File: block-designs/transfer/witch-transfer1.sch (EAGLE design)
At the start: 13 parts, among them IC1 74LS73N, IC2 74S08N

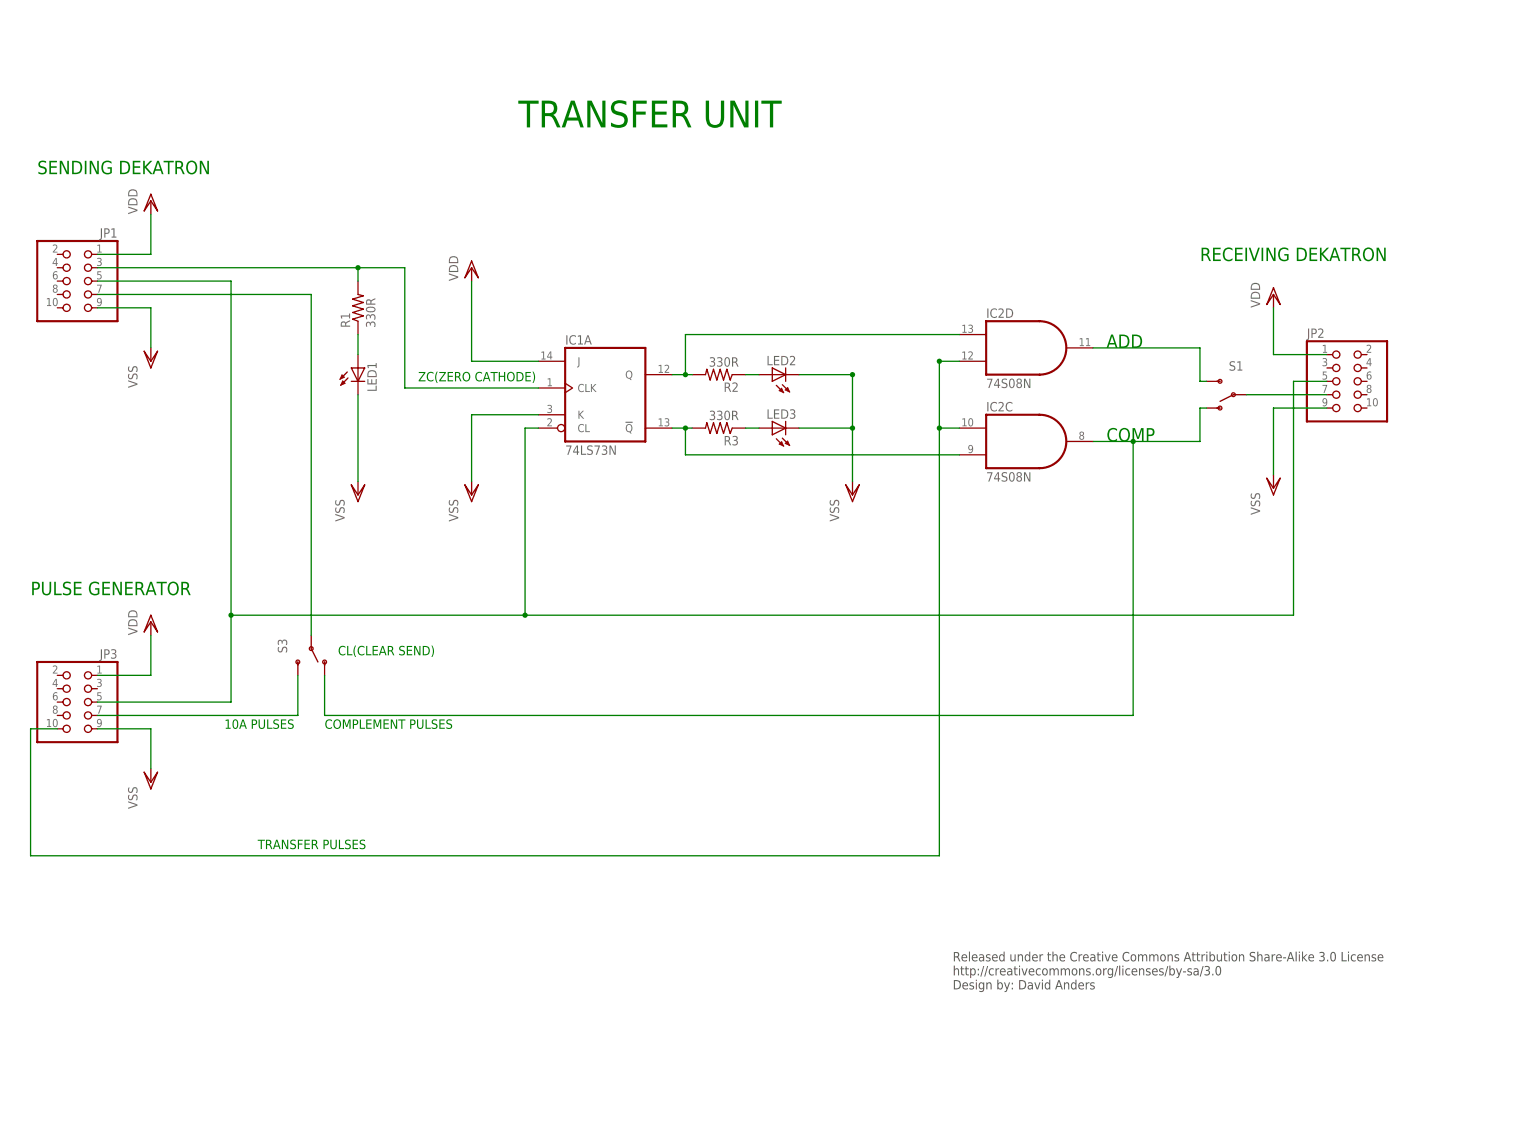
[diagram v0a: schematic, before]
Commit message: updated transfer block with board layout
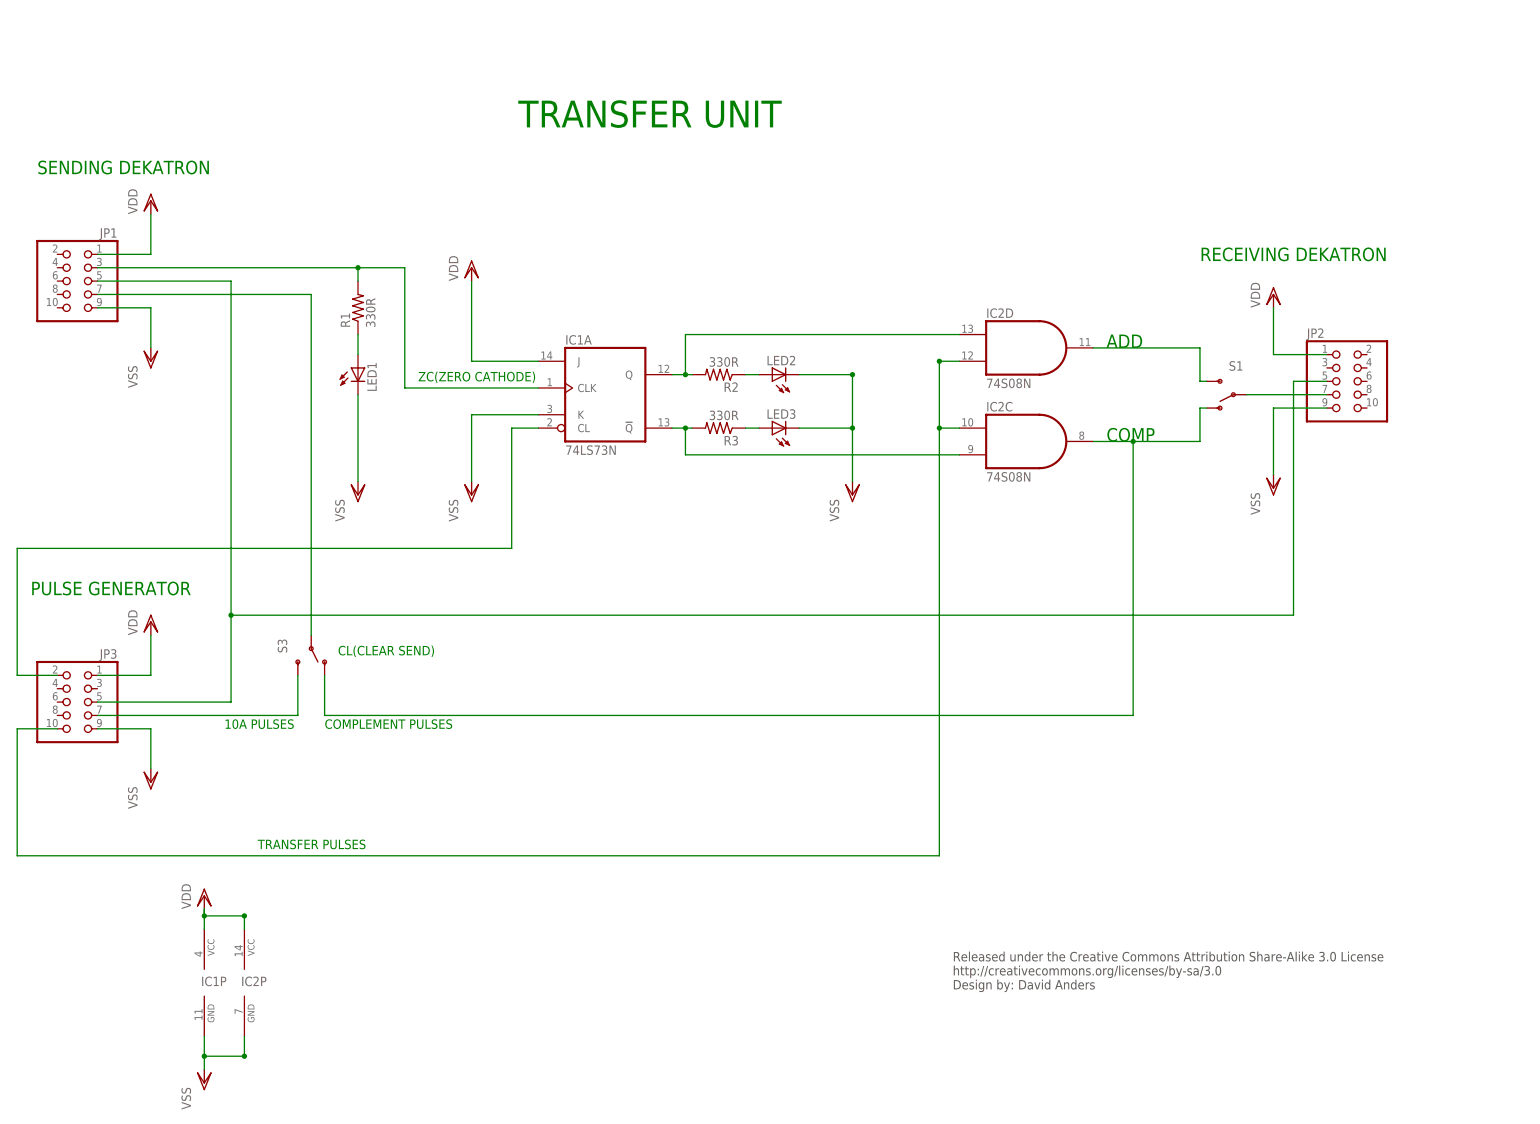
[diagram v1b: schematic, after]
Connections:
- new net N$10: IC1A.CL, JP3.2
- net N$32: no longer IC1A.CL
- net VDD: now also IC1P.VCC, IC2P.VCC
- net VSS: now also IC1P.GND, IC2P.GND
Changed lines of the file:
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@@
 <part name="R2" library="resistor" deviceset="R-US_" device="0204/5" value="330R"/>
 <part name="R3" library="resistor" deviceset="R-US_" device="0204/5" value="330R"/>
+<part name="VSS7" library="supply1" deviceset="VSS" device=""/>
+<part name="VDD5" library="supply1" deviceset="VDD" device=""/>
 </parts>
 <sheets>
@@
 <instance part="R2" gate="G$1" x="140.97" y="142.24" rot="R180"/>
 <instance part="R3" gate="G$1" x="140.97" y="132.08" rot="R180"/>
+<instance part="IC1" gate="P" x="43.18" y="26.67"/>
+<instance part="IC2" gate="P" x="50.8" y="26.67"/>
+<instance part="VSS7" gate="G$1" x="43.18" y="7.62"/>
+<instance part="VDD5" gate="G$1" x="43.18" y="43.18"/>
 </instances>
 <busses>
@@
 <net name="N$32" class="0">
 <segment>
-<pinref part="IC1" gate="A" pin="CL"/>
-<wire x1="106.68" y1="132.08" x2="104.14" y2="132.08" width="0.1524" layer="91"/>
 <pinref part="JP1" gate="A" pin="5"/>
 <wire x1="22.86" y1="160.02" x2="48.26" y2="160.02" width="0.1524" layer="91"/>
@@
 <wire x1="48.26" y1="160.02" x2="48.26" y2="96.52" width="0.1524" layer="91"/>
 <wire x1="48.26" y1="96.52" x2="48.26" y2="80.01" width="0.1524" layer="91"/>
-<wire x1="104.14" y1="132.08" x2="104.14" y2="96.52" width="0.1524" layer="91"/>
-<wire x1="104.14" y1="96.52" x2="48.26" y2="96.52" width="0.1524" layer="91"/>
 <junction x="48.26" y="96.52"/>
-<wire x1="104.14" y1="96.52" x2="250.19" y2="96.52" width="0.1524" layer="91"/>
+<wire x1="48.26" y1="96.52" x2="250.19" y2="96.52" width="0.1524" layer="91"/>
 <wire x1="250.19" y1="96.52" x2="250.19" y2="140.97" width="0.1524" layer="91"/>
-<junction x="104.14" y="96.52"/>
 <pinref part="JP2" gate="A" pin="5"/>
 <wire x1="256.54" y1="140.97" x2="250.19" y2="140.97" width="0.1524" layer="91"/>
 </segment>
 </net>
+<net name="N$2" class="0">
+<segment>
+<pinref part="IC2" gate="D" pin="I0"/>
+<wire x1="186.69" y1="144.78" x2="182.88" y2="144.78" width="0.1524" layer="91"/>
+<junction x="182.88" y="144.78"/>
+<pinref part="IC2" gate="C" pin="I1"/>
+<wire x1="186.69" y1="132.08" x2="182.88" y2="132.08" width="0.1524" layer="91"/>
+<wire x1="182.88" y1="132.08" x2="182.88" y2="144.78" width="0.1524" layer="91"/>
+<pinref part="JP3" gate="A" pin="10"/>
+<wire x1="15.24" y1="74.93" x2="7.62" y2="74.93" width="0.1524" layer="91"/>
+<wire x1="7.62" y1="74.93" x2="7.62" y2="50.8" width="0.1524" layer="91"/>
+<wire x1="7.62" y1="50.8" x2="182.88" y2="50.8" width="0.1524" layer="91"/>
+<wire x1="182.88" y1="50.8" x2="182.88" y2="132.08" width="0.1524" layer="91"/>
+<junction x="182.88" y="132.08"/>
+</segment>
+</net>
+<net name="N$1" class="0">
+<segment>
+<pinref part="S1" gate="1" pin="P"/>
+<pinref part="JP2" gate="A" pin="7"/>
+<wire x1="241.3" y1="138.43" x2="256.54" y2="138.43" width="0.1524" layer="91"/>
+</segment>
+</net>
+<net name="N$9" class="0">
+<segment>
+<wire x1="22.86" y1="77.47" x2="60.96" y2="77.47" width="0.1524" layer="91"/>
+<pinref part="JP3" gate="A" pin="7"/>
+<pinref part="S3" gate="1" pin="S"/>
+<wire x1="60.96" y1="77.47" x2="60.96" y2="85.09" width="0.1524" layer="91"/>
+</segment>
+</net>
+<net name="N$6" class="0">
+<segment>
+<pinref part="R2" gate="G$1" pin="1"/>
+<pinref part="LED2" gate="G$1" pin="A"/>
+<wire x1="146.05" y1="142.24" x2="148.59" y2="142.24" width="0.1524" layer="91"/>
+</segment>
+</net>
+<net name="N$7" class="0">
+<segment>
+<pinref part="R3" gate="G$1" pin="1"/>
+<pinref part="LED3" gate="G$1" pin="A"/>
+<wire x1="146.05" y1="132.08" x2="148.59" y2="132.08" width="0.1524" layer="91"/>
+</segment>
+</net>
+<net name="N$8" class="0">
+<segment>
+<pinref part="LED1" gate="G$1" pin="A"/>
+<pinref part="R1" gate="G$1" pin="1"/>
+<wire x1="72.39" y1="146.05" x2="72.39" y2="149.86" width="0.1524" layer="91"/>
+</segment>
+</net>
 <net name="VDD" class="0">
+<segment>
+<pinref part="IC1" gate="P" pin="VCC"/>
+<pinref part="VDD5" gate="G$1" pin="VDD"/>
+<wire x1="43.18" y1="36.83" x2="43.18" y2="39.37" width="0.1524" layer="91"/>
+<wire x1="43.18" y1="39.37" x2="43.18" y2="40.64" width="0.1524" layer="91"/>
+<wire x1="43.18" y1="40.64" x2="43.18" y2="39.37" width="0.1524" layer="91"/>
+<pinref part="IC2" gate="P" pin="VCC"/>
+<wire x1="43.18" y1="39.37" x2="50.8" y2="39.37" width="0.1524" layer="91"/>
+<wire x1="50.8" y1="39.37" x2="50.8" y2="36.83" width="0.1524" layer="91"/>
+<junction x="43.18" y="39.37"/>
+<junction x="50.8" y="39.37"/>
+</segment>
 <segment>
 <pinref part="JP2" gate="A" pin="1"/>
@@
 </net>
 <net name="VSS" class="0">
+<segment>
+<pinref part="VSS7" gate="G$1" pin="VSS"/>
+<pinref part="IC1" gate="P" pin="GND"/>
+<wire x1="43.18" y1="10.16" x2="43.18" y2="12.7" width="0.1524" layer="91"/>
+<pinref part="IC2" gate="P" pin="GND"/>
+<wire x1="43.18" y1="12.7" x2="43.18" y2="16.51" width="0.1524" layer="91"/>
+<wire x1="43.18" y1="12.7" x2="50.8" y2="12.7" width="0.1524" layer="91"/>
+<wire x1="50.8" y1="12.7" x2="50.8" y2="16.51" width="0.1524" layer="91"/>
+<junction x="43.18" y="12.7"/>
+<junction x="50.8" y="12.7"/>
+</segment>
 <segment>
 <pinref part="JP1" gate="A" pin="9"/>
@@
 </segment>
 </net>
-<net name="N$2" class="0">
-<segment>
-<pinref part="IC2" gate="D" pin="I0"/>
-<wire x1="186.69" y1="144.78" x2="182.88" y2="144.78" width="0.1524" layer="91"/>
-<junction x="182.88" y="144.78"/>
-<pinref part="IC2" gate="C" pin="I1"/>
-<wire x1="186.69" y1="132.08" x2="182.88" y2="132.08" width="0.1524" layer="91"/>
-<wire x1="182.88" y1="132.08" x2="182.88" y2="144.78" width="0.1524" layer="91"/>
-<pinref part="JP3" gate="A" pin="10"/>
-<wire x1="15.24" y1="74.93" x2="10.16" y2="74.93" width="0.1524" layer="91"/>
-<wire x1="10.16" y1="74.93" x2="10.16" y2="50.8" width="0.1524" layer="91"/>
-<wire x1="10.16" y1="50.8" x2="182.88" y2="50.8" width="0.1524" layer="91"/>
-<wire x1="182.88" y1="50.8" x2="182.88" y2="132.08" width="0.1524" layer="91"/>
-<junction x="182.88" y="132.08"/>
-</segment>
-</net>
-<net name="N$1" class="0">
-<segment>
-<pinref part="S1" gate="1" pin="P"/>
-<pinref part="JP2" gate="A" pin="7"/>
-<wire x1="241.3" y1="138.43" x2="256.54" y2="138.43" width="0.1524" layer="91"/>
-</segment>
-</net>
-<net name="N$9" class="0">
-<segment>
-<wire x1="22.86" y1="77.47" x2="60.96" y2="77.47" width="0.1524" layer="91"/>
-<pinref part="JP3" gate="A" pin="7"/>
-<pinref part="S3" gate="1" pin="S"/>
-<wire x1="60.96" y1="77.47" x2="60.96" y2="85.09" width="0.1524" layer="91"/>
-</segment>
-</net>
-<net name="N$6" class="0">
-<segment>
-<pinref part="R2" gate="G$1" pin="1"/>
-<pinref part="LED2" gate="G$1" pin="A"/>
-<wire x1="146.05" y1="142.24" x2="148.59" y2="142.24" width="0.1524" layer="91"/>
-</segment>
-</net>
-<net name="N$7" class="0">
-<segment>
-<pinref part="R3" gate="G$1" pin="1"/>
-<pinref part="LED3" gate="G$1" pin="A"/>
-<wire x1="146.05" y1="132.08" x2="148.59" y2="132.08" width="0.1524" layer="91"/>
-</segment>
-</net>
-<net name="N$8" class="0">
-<segment>
-<pinref part="LED1" gate="G$1" pin="A"/>
-<pinref part="R1" gate="G$1" pin="1"/>
-<wire x1="72.39" y1="146.05" x2="72.39" y2="149.86" width="0.1524" layer="91"/>
-</segment>
-</net>
+<net name="N$10" class="0">
+<segment>
+<pinref part="IC1" gate="A" pin="CL"/>
+<wire x1="106.68" y1="132.08" x2="101.6" y2="132.08" width="0.1524" layer="91"/>
+<wire x1="101.6" y1="132.08" x2="101.6" y2="109.22" width="0.1524" layer="91"/>
+<wire x1="101.6" y1="109.22" x2="7.62" y2="109.22" width="0.1524" layer="91"/>
+<wire x1="7.62" y1="109.22" x2="7.62" y2="85.09" width="0.1524" layer="91"/>
+<pinref part="JP3" gate="A" pin="2"/>
+<wire x1="15.24" y1="85.09" x2="7.62" y2="85.09" width="0.1524" layer="91"/>
+</segment>
+</net>

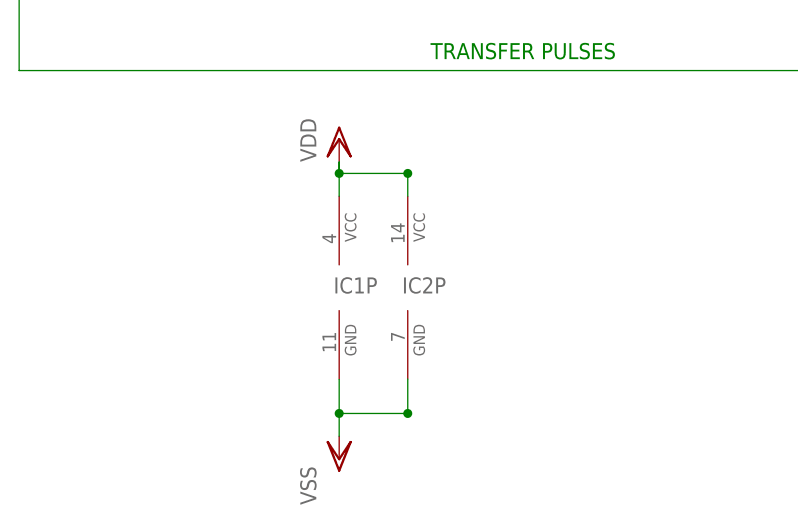
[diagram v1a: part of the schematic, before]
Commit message: updated schematics and layouts for phase 1 block designs
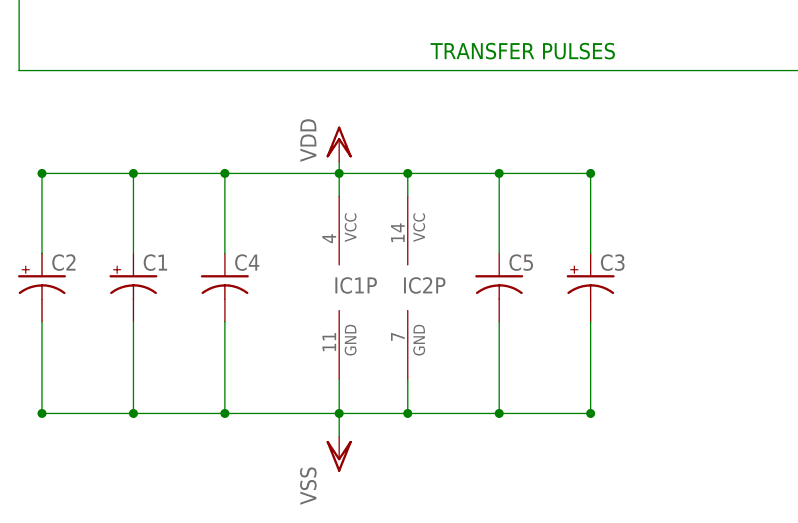
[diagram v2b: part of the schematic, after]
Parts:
- added C1, C2, C3: (no value), resistor:CPOL-USE2-5
- added C4, C5: (no value), resistor:C-US025-025X050
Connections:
- net VDD: now also C1.+, C2.+, C3.+, C4.1, C5.1
- net VSS: now also C1.-, C2.-, C3.-, C4.2, C5.2
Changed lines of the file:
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@@
 <setting verticaltext="up"/>
 </settings>
-<grid distance="0.05" unitdist="inch" unit="inch" style="lines" multiple="1" display="no" altdistance="0.01" altunitdist="inch" altunit="inch"/>
+<grid distance="0.1" unitdist="inch" unit="inch" style="lines" multiple="1" display="no" altdistance="0.01" altunitdist="inch" altunit="inch"/>
 <layers>
 <layer number="1" name="Top" color="4" fill="1" visible="no" active="no"/>
@@
 <part name="VSS7" library="supply1" deviceset="VSS" device=""/>
 <part name="VDD5" library="supply1" deviceset="VDD" device=""/>
+<part name="C1" library="resistor" deviceset="CPOL-US" device="E2-5"/>
+<part name="C2" library="resistor" deviceset="CPOL-US" device="E2-5"/>
+<part name="C3" library="resistor" deviceset="CPOL-US" device="E2-5"/>
+<part name="C4" library="resistor" deviceset="C-US" device="025-025X050"/>
+<part name="C5" library="resistor" deviceset="C-US" device="025-025X050"/>
 </parts>
 <sheets>
@@
 <instance part="VSS7" gate="G$1" x="43.18" y="7.62"/>
 <instance part="VDD5" gate="G$1" x="43.18" y="43.18"/>
+<instance part="C1" gate="G$1" x="20.32" y="27.94"/>
+<instance part="C2" gate="G$1" x="10.16" y="27.94"/>
+<instance part="C3" gate="G$1" x="71.12" y="27.94"/>
+<instance part="C4" gate="G$1" x="30.48" y="27.94"/>
+<instance part="C5" gate="G$1" x="60.96" y="27.94"/>
 </instances>
 <busses>
@@
 <pinref part="VDD5" gate="G$1" pin="VDD"/>
 <wire x1="43.18" y1="36.83" x2="43.18" y2="39.37" width="0.1524" layer="91"/>
-<wire x1="43.18" y1="39.37" x2="43.18" y2="40.64" width="0.1524" layer="91"/>
 <wire x1="43.18" y1="40.64" x2="43.18" y2="39.37" width="0.1524" layer="91"/>
 <pinref part="IC2" gate="P" pin="VCC"/>
@@
 <junction x="43.18" y="39.37"/>
 <junction x="50.8" y="39.37"/>
+<pinref part="C3" gate="G$1" pin="+"/>
+<wire x1="50.8" y1="39.37" x2="60.96" y2="39.37" width="0.1524" layer="91"/>
+<wire x1="60.96" y1="39.37" x2="71.12" y2="39.37" width="0.1524" layer="91"/>
+<wire x1="71.12" y1="39.37" x2="71.12" y2="30.48" width="0.1524" layer="91"/>
+<pinref part="C5" gate="G$1" pin="1"/>
+<wire x1="60.96" y1="30.48" x2="60.96" y2="39.37" width="0.1524" layer="91"/>
+<junction x="60.96" y="39.37"/>
+<junction x="71.12" y="39.37"/>
+<pinref part="C2" gate="G$1" pin="+"/>
+<wire x1="43.18" y1="39.37" x2="30.48" y2="39.37" width="0.1524" layer="91"/>
+<wire x1="30.48" y1="39.37" x2="20.32" y2="39.37" width="0.1524" layer="91"/>
+<wire x1="20.32" y1="39.37" x2="10.16" y2="39.37" width="0.1524" layer="91"/>
+<wire x1="10.16" y1="39.37" x2="10.16" y2="30.48" width="0.1524" layer="91"/>
+<pinref part="C1" gate="G$1" pin="+"/>
+<wire x1="20.32" y1="30.48" x2="20.32" y2="39.37" width="0.1524" layer="91"/>
+<pinref part="C4" gate="G$1" pin="1"/>
+<wire x1="30.48" y1="30.48" x2="30.48" y2="39.37" width="0.1524" layer="91"/>
+<junction x="10.16" y="39.37"/>
+<junction x="20.32" y="39.37"/>
+<junction x="30.48" y="39.37"/>
 </segment>
 <segment>
@@
 <junction x="43.18" y="12.7"/>
 <junction x="50.8" y="12.7"/>
-</segment>
-<segment>
+<pinref part="C3" gate="G$1" pin="-"/>
+<wire x1="50.8" y1="12.7" x2="60.96" y2="12.7" width="0.1524" layer="91"/>
+<wire x1="60.96" y1="12.7" x2="71.12" y2="12.7" width="0.1524" layer="91"/>
+<wire x1="71.12" y1="12.7" x2="71.12" y2="22.86" width="0.1524" layer="91"/>
+<pinref part="C5" gate="G$1" pin="2"/>
+<wire x1="60.96" y1="22.86" x2="60.96" y2="12.7" width="0.1524" layer="91"/>
+<junction x="60.96" y="12.7"/>
+<junction x="71.12" y="12.7"/>
+<pinref part="C2" gate="G$1" pin="-"/>
+<wire x1="10.16" y1="22.86" x2="10.16" y2="12.7" width="0.1524" layer="91"/>
+<wire x1="10.16" y1="12.7" x2="20.32" y2="12.7" width="0.1524" layer="91"/>
+<pinref part="C1" gate="G$1" pin="-"/>
+<wire x1="20.32" y1="12.7" x2="30.48" y2="12.7" width="0.1524" layer="91"/>
+<wire x1="30.48" y1="12.7" x2="43.18" y2="12.7" width="0.1524" layer="91"/>
+<wire x1="20.32" y1="22.86" x2="20.32" y2="12.7" width="0.1524" layer="91"/>
+<pinref part="C4" gate="G$1" pin="2"/>
+<wire x1="30.48" y1="22.86" x2="30.48" y2="12.7" width="0.1524" layer="91"/>
+<junction x="10.16" y="12.7"/>
+<junction x="20.32" y="12.7"/>
+<junction x="30.48" y="12.7"/>
+</segment>
+<segment>

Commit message: updated files with new images
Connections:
- removed net N$10: IC1A.CL, JP3.2
- new net N$11: IC1B.CLK, JP2.3
- new net N$12: IC1B.Q, R1.2
- new net RESET: IC1A.CL, IC1B.CL, JP3.2
- net VDD: now also IC1B.J
- net VSS: now also IC1B.K
- net ZC_TX: no longer R1.2
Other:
- moved on the sheet: C1, C2, C3, C4, C5, IC1A, IC1P, IC2C, IC2D, IC2P, JP1, JP2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
